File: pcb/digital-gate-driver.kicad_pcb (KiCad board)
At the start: 2 copper layers, 27 parts, among them J1 Conn_01x01_Pin, J2 Conn_01x06_Pin, J3 Conn_01x02_Socket, Q1 FDP61N20, U1 INA180A1, U2 TLV1871, U3 UCC27531

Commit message: update header fp
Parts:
- J1: footprint Connector_PinHeader_2.54mm:PinHeader_2x01_P2.54mm_Vertical -> Connector_PinHeader_2.54mm:PinHeader_1x01_P2.54mm_Vertical
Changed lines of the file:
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@@
 		)
 	)
-	(footprint "Connector_PinHeader_2.54mm:PinHeader_2x01_P2.54mm_Vertical"
+	(footprint "Connector_PinHeader_2.54mm:PinHeader_1x01_P2.54mm_Vertical"
 		(layer "F.Cu")
 		(at 123.25 100.68)
-		(descr "Through hole straight pin header, 2x01, 2.54mm pitch, double rows")
-		(tags "Through hole pin header THT 2x01 2.54mm double row")
+		(descr "Through hole straight pin header, 1x01, 2.54mm pitch, single row")
+		(tags "Through hole pin header THT 1x01 2.54mm single row")
 		(property "Reference" "J1"
-			(at 1.27 -2.33 0)
+			(at 0 -2.33 0)
 			(layer "F.SilkS")
 			(effects
@@
 		)
 		(property "Value" "Conn_01x01_Pin"
-			(at 1.27 2.33 0)
+			(at 0 2.33 0)
 			(layer "F.Fab")
 			(effects
@@
 			)
 		)
-		(property "Footprint" "Connector_PinHeader_2.54mm:PinHeader_2x01_P2.54mm_Vertical"
+		(property "Footprint" "Connector_PinHeader_2.54mm:PinHeader_1x01_P2.54mm_Vertical"
 			(at 0 0 0)
 			(unlocked yes)
@@
 		(fp_line
 			(start -1.33 1.27)
-			(end 1.27 1.27)
+			(end 1.33 1.27)
 			(stroke
 				(width 0.12)
@@
 		(fp_line
 			(start -1.33 1.33)
-			(end 3.87 1.33)
-			(stroke
-				(width 0.12)
-				(type solid)
-			)
-			(layer "F.SilkS")
-		)
-		(fp_line
-			(start 1.27 -1.33)
-			(end 3.87 -1.33)
-			(stroke
-				(width 0.12)
-				(type solid)
-			)
-			(layer "F.SilkS")
-		)
-		(fp_line
-			(start 1.27 1.27)
-			(end 1.27 -1.33)
-			(stroke
-				(width 0.12)
-				(type solid)
-			)
-			(layer "F.SilkS")
-		)
-		(fp_line
-			(start 3.87 -1.33)
-			(end 3.87 1.33)
+			(end 1.33 1.33)
+			(stroke
+				(width 0.12)
+				(type solid)
+			)
+			(layer "F.SilkS")
+		)
+		(fp_line
+			(start 1.33 1.27)
+			(end 1.33 1.33)
 			(stroke
 				(width 0.12)
@@
 		(fp_line
 			(start -1.8 1.8)
-			(end 4.35 1.8)
-			(stroke
-				(width 0.05)
-				(type solid)
-			)
-			(layer "F.CrtYd")
-		)
-		(fp_line
-			(start 4.35 -1.8)
+			(end 1.8 1.8)
+			(stroke
+				(width 0.05)
+				(type solid)
+			)
+			(layer "F.CrtYd")
+		)
+		(fp_line
+			(start 1.8 -1.8)
 			(end -1.8 -1.8)
 			(stroke
@@
 		)
 		(fp_line
-			(start 4.35 1.8)
-			(end 4.35 -1.8)
-			(stroke
-				(width 0.05)
-				(type solid)
-			)
-			(layer "F.CrtYd")
-		)
-		(fp_line
-			(start -1.27 0)
-			(end 0 -1.27)
+			(start 1.8 1.8)
+			(end 1.8 -1.8)
+			(stroke
+				(width 0.05)
+				(type solid)
+			)
+			(layer "F.CrtYd")
+		)
+		(fp_line
+			(start -1.27 -0.635)
+			(end -0.635 -1.27)
 			(stroke
 				(width 0.1)
@@
 		(fp_line
 			(start -1.27 1.27)
-			(end -1.27 0)
-			(stroke
-				(width 0.1)
-				(type solid)
-			)
-			(layer "F.Fab")
-		)
-		(fp_line
-			(start 0 -1.27)
-			(end 3.81 -1.27)
-			(stroke
-				(width 0.1)
-				(type solid)
-			)
-			(layer "F.Fab")
-		)
-		(fp_line
-			(start 3.81 -1.27)
-			(end 3.81 1.27)
-			(stroke
-				(width 0.1)
-				(type solid)
-			)
-			(layer "F.Fab")
-		)
-		(fp_line
-			(start 3.81 1.27)
+			(end -1.27 -0.635)
+			(stroke
+				(width 0.1)
+				(type solid)
+			)
+			(layer "F.Fab")
+		)
+		(fp_line
+			(start -0.635 -1.27)
+			(end 1.27 -1.27)
+			(stroke
+				(width 0.1)
+				(type solid)
+			)
+			(layer "F.Fab")
+		)
+		(fp_line
+			(start 1.27 -1.27)
+			(end 1.27 1.27)
+			(stroke
+				(width 0.1)
+				(type solid)
+			)
+			(layer "F.Fab")
+		)
+		(fp_line
+			(start 1.27 1.27)
 			(end -1.27 1.27)
 			(stroke
@@
 		)
 		(fp_text user "${REFERENCE}"
-			(at 1.27 0 90)
+			(at 0 0 90)
 			(layer "F.Fab")
 			(effects
@@
 			(pintype "passive")
 		)
-		(pad "2" thru_hole oval
-			(at 2.54 0)
-			(size 1.7 1.7)
-			(drill 1)
-			(layers "*.Cu" "*.Mask")
-			(remove_unused_layers no)
-		)
-		(model "${KICAD8_3DMODEL_DIR}/Connector_PinHeader_2.54mm.3dshapes/PinHeader_2x01_P2.54mm_Vertical.wrl"
+		(model "${KICAD8_3DMODEL_DIR}/Connector_PinHeader_2.54mm.3dshapes/PinHeader_1x01_P2.54mm_Vertical.wrl"
 			(offset
 				(xyz 0 0 0)

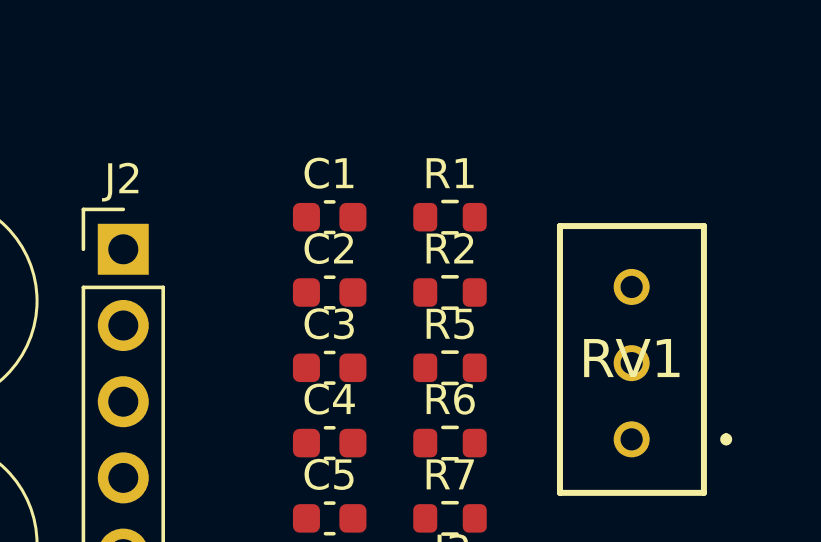
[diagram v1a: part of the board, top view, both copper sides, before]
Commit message: update shunt resistor sizes
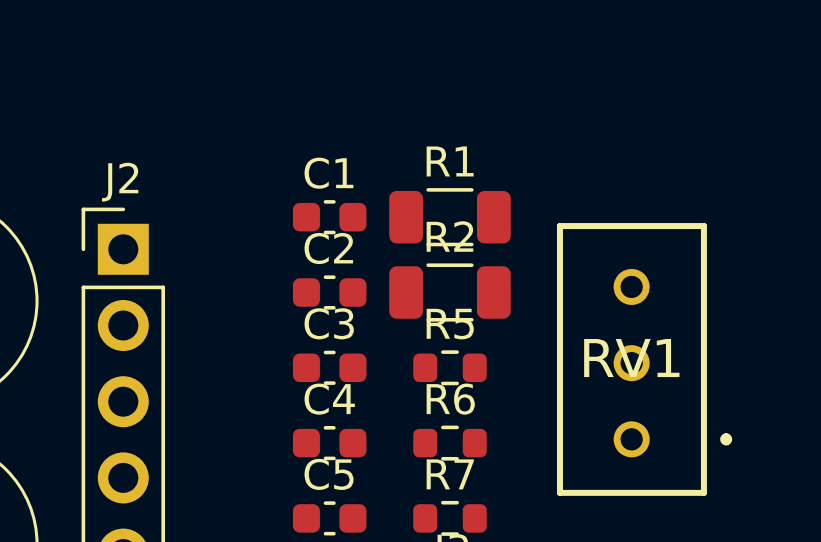
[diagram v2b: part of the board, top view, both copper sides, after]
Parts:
- R1, R2: footprint Resistor_SMD:R_0603_1608Metric -> Resistor_SMD:R_1206_3216Metric

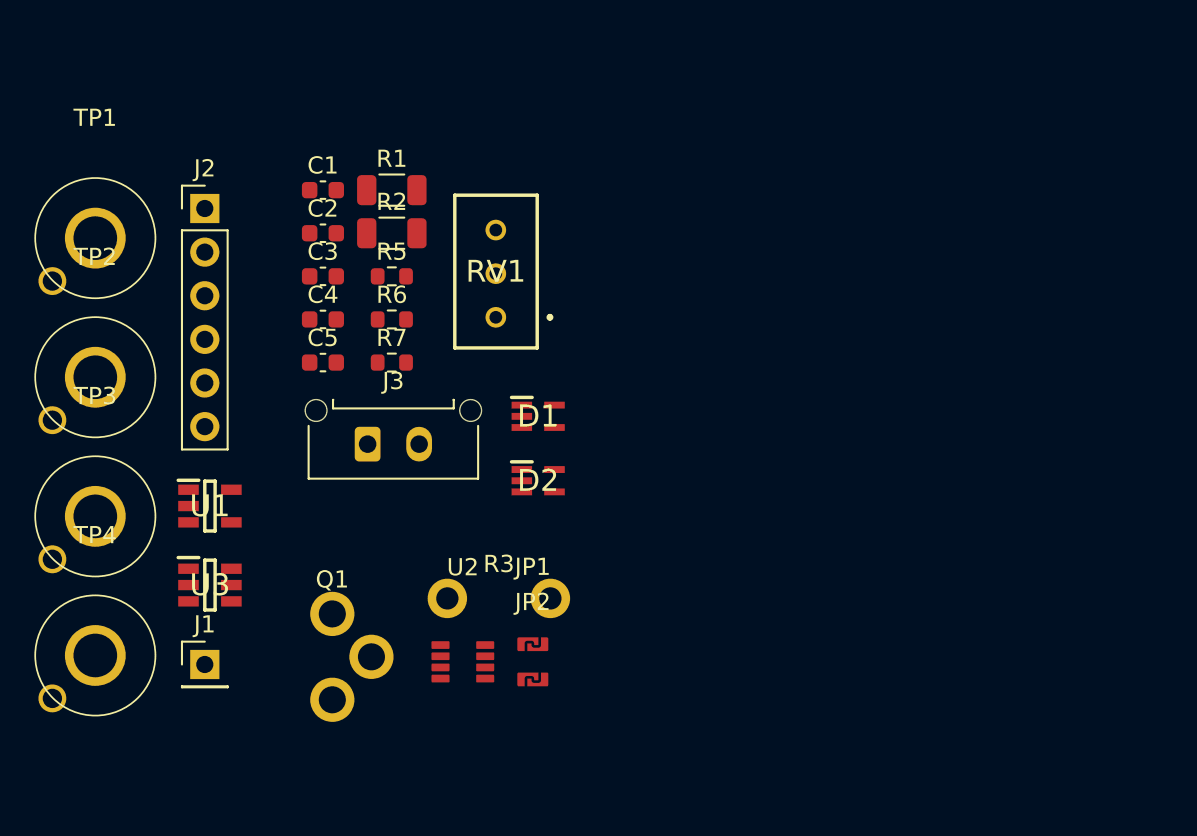
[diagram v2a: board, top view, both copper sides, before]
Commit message: add all footprints
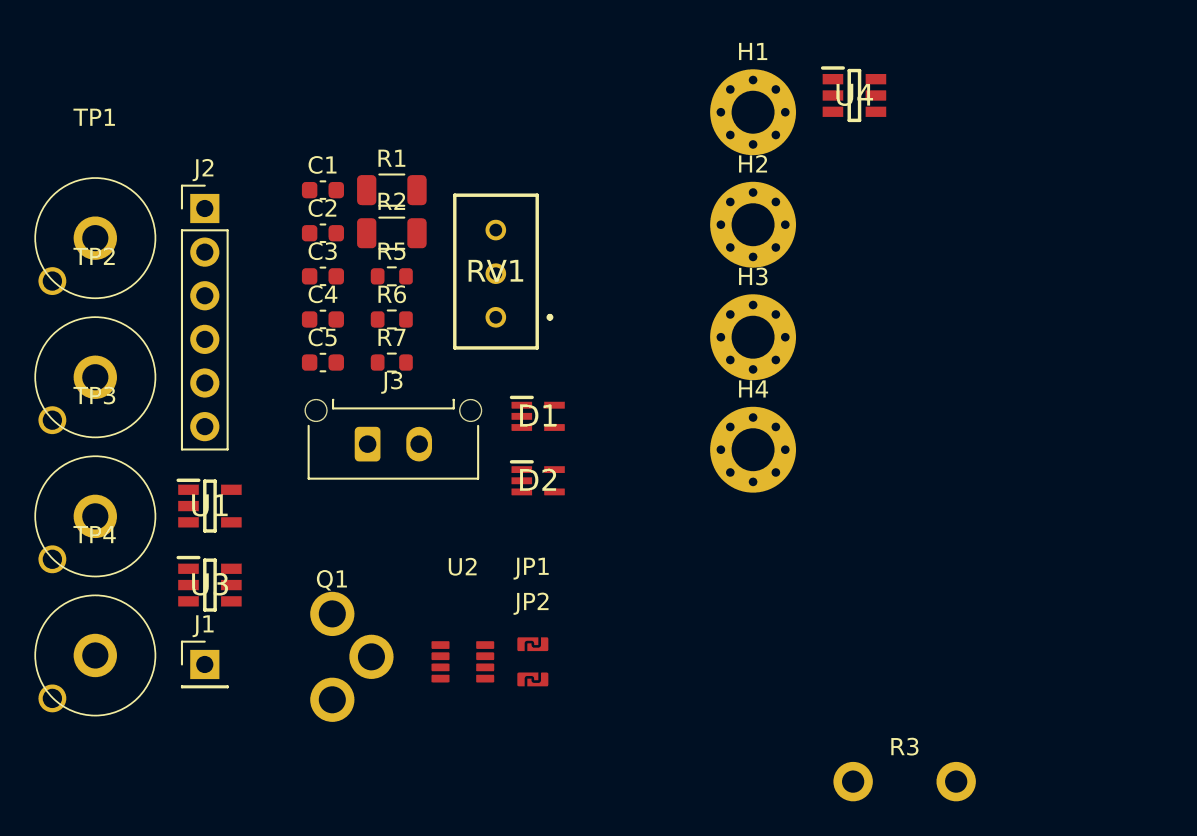
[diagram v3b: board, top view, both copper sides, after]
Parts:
- added H1: MountingHole_Pad, MountingHole:MountingHole_2.5mm_Pad_Via, F.Cu at (155.2, 68.5)
- added H2: MountingHole_Pad, MountingHole:MountingHole_2.5mm_Pad_Via, F.Cu at (155.2, 75.1)
- added H3: MountingHole_Pad, MountingHole:MountingHole_2.5mm_Pad_Via, F.Cu at (155.2, 81.6)
- added H4: MountingHole_Pad, MountingHole:MountingHole_2.5mm_Pad_Via, F.Cu at (155.2, 88.2)
- added U4: UCC27531, digital-gate-driver:UCC2753DBVT, F.Cu at (161.1, 67.5)
- moved R3 25.9 mm to (164.0, 107.5)

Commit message: complete layout
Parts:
- removed J1: Conn_01x01_Pin, Connector_PinHeader_2.54mm:PinHeader_1x01_P2.54mm_Vertical
- removed J3: Conn_01x02_Socket, Connector_Molex:Molex_Micro-Fit_3.0_43650-0215_1x02_P3.00mm_Vertical
- removed U3: UCC27531, digital-gate-driver:UCC2753DBVT
- added J5: Conn_01x04_Socket, digital-gate-driver:MOLEX_436500418, F.Cu at (174.0, 95.3)
- added TP5: TestPoint_Probe, digital-gate-driver:TP_SMD, F.Cu at (150.6, 91.6)
- added TP6: TestPoint_Probe, digital-gate-driver:TP_SMD, F.Cu at (157.5, 81.3)
- added TP7: TestPoint_Probe, digital-gate-driver:TP_SMD, F.Cu at (157.6, 87.3)
- moved TP1 50.0 mm to (166.6, 80.8)
- moved TP4 49.8 mm to (166.6, 100.8)
- moved R1 38.7 mm to (159.8, 102.0)
- moved U1 37.1 mm to (159.8, 99.0)
- moved Q1 34.1 mm to (160.5, 83.8), turned to 180 degrees
- moved C5 32.5 mm to (159.8, 96.4)
- moved C4 30.5 mm to (152.5, 101.4)
- moved R6 29.3 mm to (156.9, 99.0), turned to 90 degrees
- moved TP3 28.9 mm to (144.4, 100.8)
- moved C3 28.5 mm to (149.5, 99.0), turned to 90 degrees
- moved H3 28.5 mm to (136.1, 102.8)
- moved TP2 27.7 mm to (144.4, 80.8)
- moved R7 26.5 mm to (155.3, 99.0), turned to 90 degrees
- moved R5 26.2 mm to (152.5, 96.8)
- moved R3 25.6 mm to (154.4, 83.8), turned to -90 degrees
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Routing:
- net VCC: track 0.00 -> 63.2 mm
- net /SECONDARY_SHUNT+: track 0.00 -> 40.3 mm, vias 0 -> 6
- net /CONDUCTION_DETECT: track 0.00 -> 36.9 mm, vias 0 -> 2
- net +3V3: track 0.00 -> 30.6 mm
- net GND: track 0.00 -> 29.3 mm, vias 0 -> 16
- net /CURRENT_AMP: track 0.00 -> 26.0 mm, vias 0 -> 2
- net /Vdrain: track 0.00 -> 24.2 mm
- net /GATE_EN: track 0.00 -> 21.0 mm, vias 0 -> 2
- net Net-(Q1-S): track 0.00 -> 20.6 mm
- net /GATE_IN: track 0.00 -> 19.7 mm, vias 0 -> 2
- net Net-(JP1-B): track 0.00 -> 12.3 mm
- net /Vref: track 0.00 -> 11.0 mm
- net Net-(JP2-A): track 0.00 -> 7.51 mm
- net Net-(JP1-A): track 0.00 -> 2.77 mm
- net Net-(R6-Pad2): track 0.00 -> 1.75 mm
- added copper zone on B.Cu, net GND
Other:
- board outline added: 44 x 30 mm
- board text added: "3V3"
- board text added: "4-22-25"
- board text added: "COND_DET"
- board text added: "CW: + CCW: -"
- board text added: "DIGITAL GATE DRIVER"
- board text added: "GATE EN"
- board text added: "GATE IN"
- board text added: "GND"
- board text added: "I_amp"
- board text added: "MC•AH•DP"
- board text added: "REV A"
- board text added: "SHUNT"
- board text added: "VCC"
- board text added: "VDRAIN"
- board text added: "Vdrain"
- board text added: "Vshunt"
- board text added: "~{COND}"

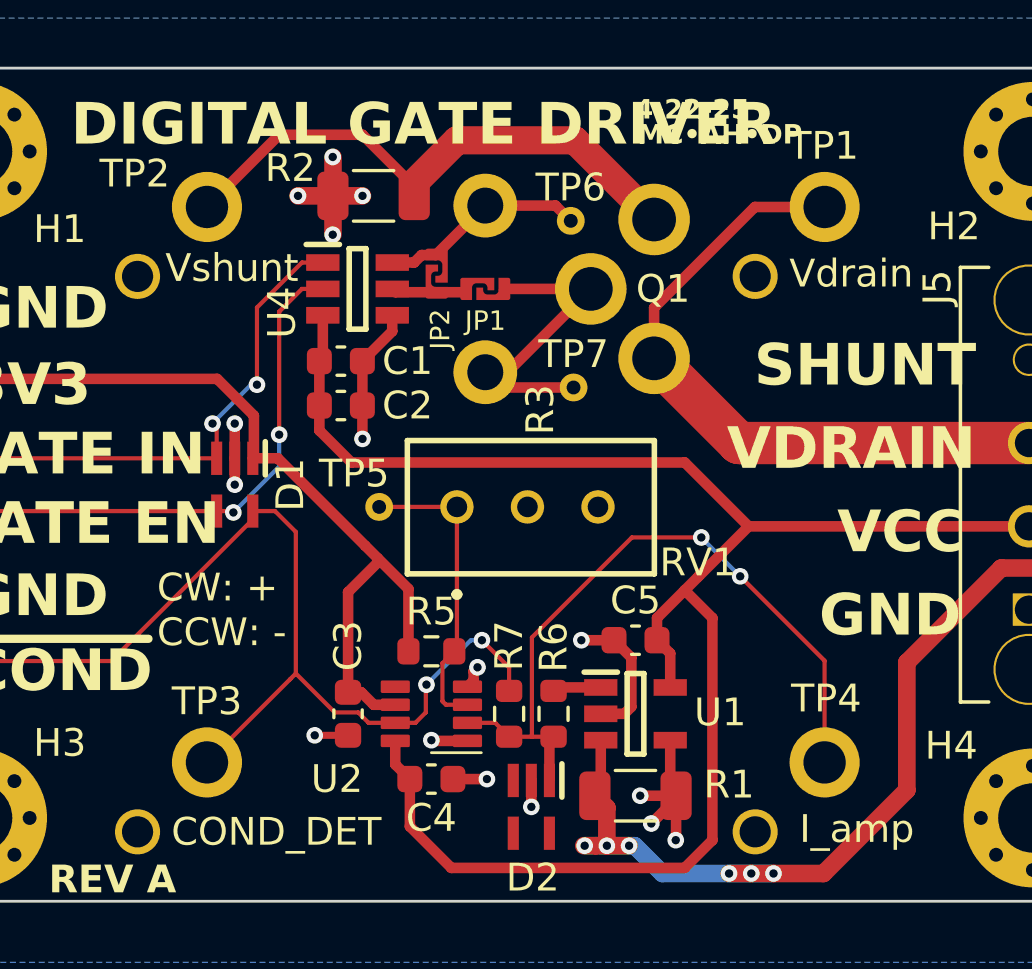
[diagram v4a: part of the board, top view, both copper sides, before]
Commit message: spec hysteresis resistors, update socket hole diameters
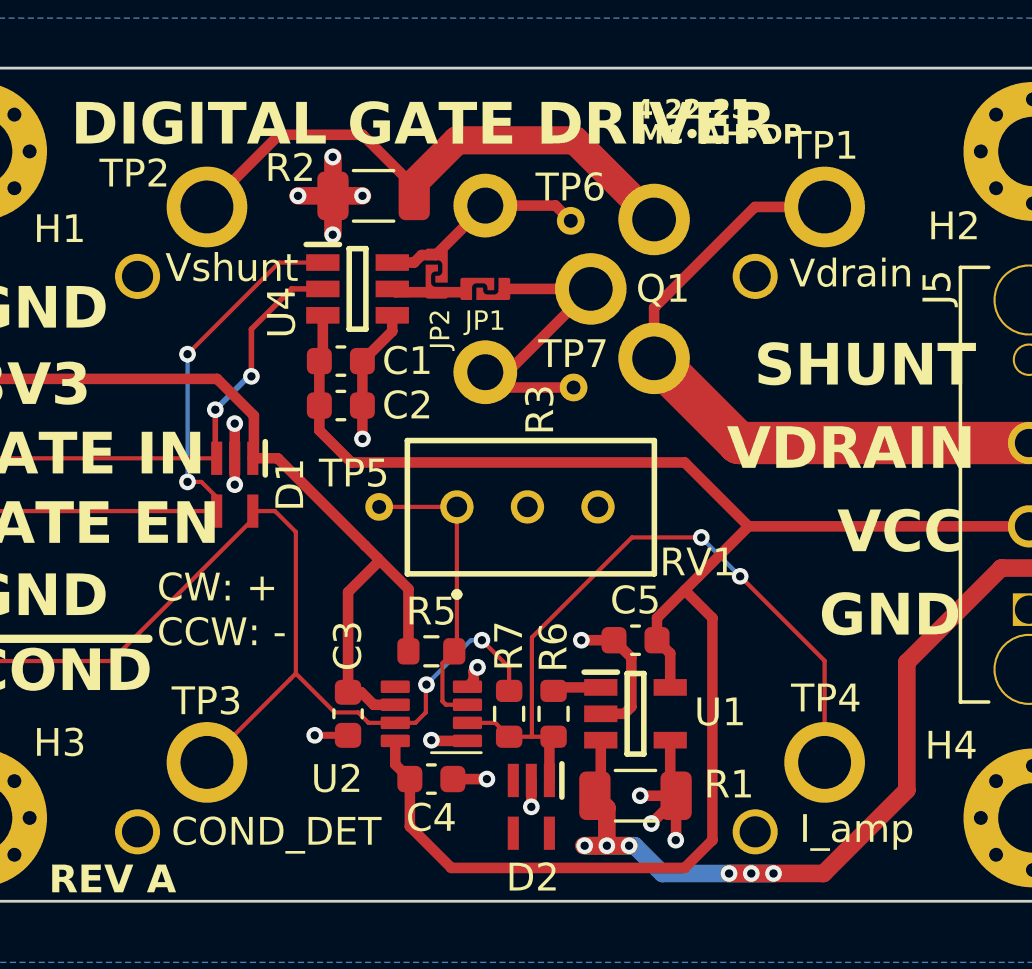
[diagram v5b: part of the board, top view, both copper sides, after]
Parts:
- R6: value ~ -> 1k
- R7: value ~ -> 32k
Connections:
- U4 pad 1: /GATE_IN -> /GATE_EN
- U4 pad 2: /GATE_EN -> /GATE_IN
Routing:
- net /GATE_EN: track 21.0 -> 23.0 mm
- net /GATE_IN: track 19.7 -> 18.8 mm
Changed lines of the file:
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@@
 		(pad "1" thru_hole circle
 			(at 0 0)
-			(size 2.524 2.524)
-			(drill 1.524)
+			(size 2.905 2.905)
+			(drill 1.905)
 			(layers "*.Cu" "*.Mask")
 			(remove_unused_layers no)
@@
 			(size 0.6 1.2)
 			(layers "F.Cu" "F.Paste" "F.Mask")
-			(net 5 "/GATE_IN")
+			(net 6 "/GATE_EN")
 			(pinfunction "EN")
 			(pintype "input")
@@
 			(size 0.6 1.2)
 			(layers "F.Cu" "F.Paste" "F.Mask")
-			(net 6 "/GATE_EN")
+			(net 5 "/GATE_IN")
 			(pinfunction "IN")
 			(pintype "input")
@@
 			)
 		)
-		(property "Value" "~"
+		(property "Value" "32k"
 			(at 0 1.43 90)
 			(layer "F.Fab")
@@
 			)
 		)
-		(property "Value" "~"
+		(property "Value" "1k"
 			(at 0 1.43 90)
 			(layer "F.Fab")
@@
 		(pad "1" thru_hole circle
 			(at 0 0)
-			(size 2.524 2.524)
-			(drill 1.524)
+			(size 2.905 2.905)
+			(drill 1.905)
 			(layers "*.Cu" "*.Mask")
 			(remove_unused_layers no)
@@
 		(pad "1" thru_hole circle
 			(at 0 0)
-			(size 2.524 2.524)
-			(drill 1.524)
+			(size 2.905 2.905)
+			(drill 1.905)
 			(layers "*.Cu" "*.Mask")
 			(remove_unused_layers no)
@@
 		(pad "1" thru_hole circle
 			(at 0 0)
-			(size 2.524 2.524)
-			(drill 1.524)
+			(size 2.905 2.905)
+			(drill 1.905)
 			(layers "*.Cu" "*.Mask")
 			(remove_unused_layers no)
@@
 	)
 	(segment
-		(start 144.75 89.85)
-		(end 134.86 89.85)
-		(width 0.1524)
+		(start 144.7 88.1)
+		(end 144.7 89.8)
+		(width 0.2)
 		(layer "F.Cu")
 		(net 5)
 	)
 	(segment
-		(start 146.2 84.419826)
-		(end 146.2 87.2)
+		(start 144.75 89.85)
+		(end 134.86 89.85)
 		(width 0.1524)
 		(layer "F.Cu")
@@
 	)
 	(segment
-		(start 147.819326 82.8005)
-		(end 146.2 84.419826)
-		(width 0.1524)
+		(start 146 85.2)
+		(end 146 86.9)
+		(width 0.2)
 		(layer "F.Cu")
 		(net 5)
 	)
 	(segment
-		(start 144.75 88.750003)
-		(end 144.599997 88.6)
-		(width 0.1524)
+		(start 144.7 89.8)
+		(end 144.75 89.85)
+		(width 0.2)
 		(layer "F.Cu")
 		(net 5)
 	)
 	(segment
-		(start 144.75 89.85)
-		(end 144.75 88.750003)
-		(width 0.1524)
+		(start 147.4495 83.7505)
+		(end 146 85.2)
+		(width 0.2)
 		(layer "F.Cu")
 		(net 5)
 	)
 	(segment
-		(start 148.571726 82.8005)
-		(end 147.819326 82.8005)
+		(start 134.86 89.85)
+		(end 134.54 89.53)
 		(width 0.1524)
 		(layer "F.Cu")
@@
 	)
 	(segment
-		(start 134.86 89.85)
-		(end 134.54 89.53)
-		(width 0.1524)
+		(start 148.571726 83.7505)
+		(end 147.4495 83.7505)
+		(width 0.2)
 		(layer "F.Cu")
 		(net 5)
 	)
 	(via
-		(at 144.599997 88.6)
+		(at 144.7 88.1)
 		(size 0.6)
 		(drill 0.3)
@@
 	)
 	(via
-		(at 146.2 87.2)
+		(at 146 86.9)
 		(size 0.6)
 		(drill 0.3)
 		(layers "F.Cu" "B.Cu")
-		(free yes)
 		(net 5)
 	)
 	(segment
-		(start 146.2 87.2)
-		(end 145.98513 87.2)
-		(width 0.1524)
+		(start 146 86.9)
+		(end 145.9 86.9)
+		(width 0.2)
 		(layer "B.Cu")
 		(net 5)
 	)
 	(segment
-		(start 144.599997 88.585133)
-		(end 144.599997 88.6)
-		(width 0.1524)
+		(start 145.9 86.9)
+		(end 144.7 88.1)
+		(width 0.2)
 		(layer "B.Cu")
 		(net 5)
 	)
 	(segment
-		(start 145.98513 87.2)
-		(end 144.599997 88.585133)
-		(width 0.1524)
-		(layer "B.Cu")
-		(net 5)
-	)
-	(segment
-		(start 145.299998 91.75)
-		(end 144.75 91.75)
+		(start 146.9995 82.8005)
+		(end 148.571726 82.8005)
 		(width 0.1524)
 		(layer "F.Cu")
@@
 	)
 	(segment
-		(start 147.819326 83.7505)
-		(end 147 84.569826)
+		(start 143.7 90.7)
+		(end 144.2 90.7)
 		(width 0.1524)
 		(layer "F.Cu")
@@
 	)
 	(segment
-		(start 147 84.569826)
-		(end 147 89)
+		(start 144.75 91.25)
+		(end 144.75 91.75)
 		(width 0.1524)
 		(layer "F.Cu")
@@
 	)
 	(segment
-		(start 145.349998 91.8)
-		(end 145.299998 91.75)
+		(start 143.7 86.1)
+		(end 146.9995 82.8005)
 		(width 0.1524)
 		(layer "F.Cu")
@@
 	)
 	(segment
-		(start 148.571726 83.7505)
-		(end 147.819326 83.7505)
-		(width 0.1524)
-		(layer "F.Cu")
-		(net 6)
-	)
-	(segment
-		(start 147 89)
-		(end 147.2 89)
+		(start 144.2 90.7)
+		(end 144.75 91.25)
 		(width 0.1524)
 		(layer "F.Cu")
@@
 	)
 	(via
-		(at 145.349998 91.8)
+		(at 143.7 86.1)
 		(size 0.6)
 		(drill 0.3)
@@
 	)
 	(via
-		(at 147 89)
+		(at 143.7 90.7)
 		(size 0.6)
 		(drill 0.3)
@@
 	)
 	(segment
-		(start 145.349998 91.8)
-		(end 147 90.149998)
-		(width 0.1524)
-		(layer "B.Cu")
-		(net 6)
-	)
-	(segment
-		(start 147 90.149998)
-		(end 147 89)
+		(start 143.7 90.7)
+		(end 143.7 86.1)
 		(width 0.1524)
 		(layer "B.Cu")
